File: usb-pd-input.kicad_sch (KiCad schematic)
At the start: 14 parts, among them J1 USB-C, Q1 -30V -4A, U1 STUSB4500QTR

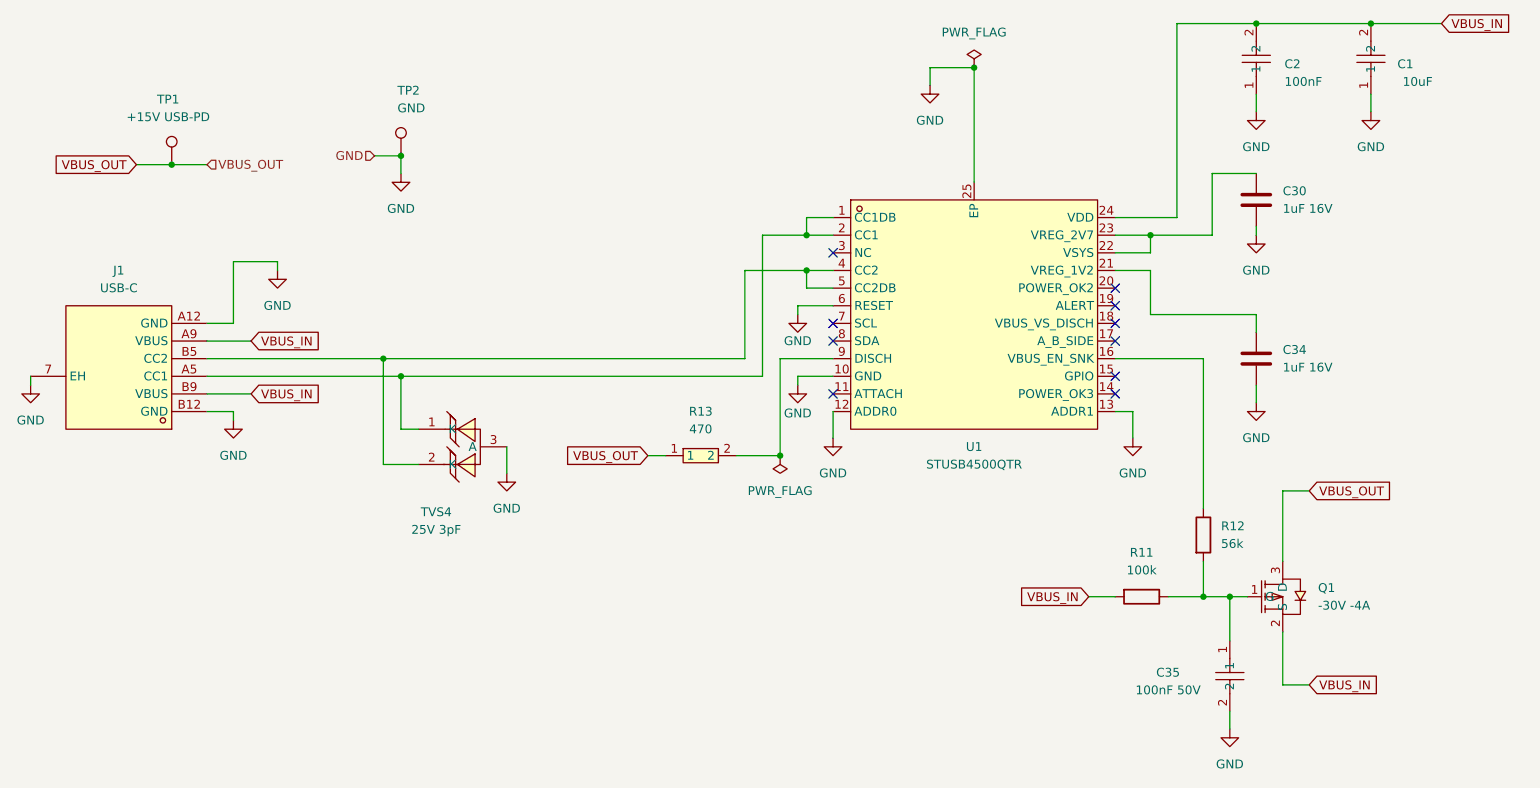
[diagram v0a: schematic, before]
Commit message: fix: Correct project name in hierarchical schematic instances
All sub-sheet instance blocks had inconsistent project names - some used
(project "") while others used (project "zudo-pd"). This caused KiCad to
display "?" for designators when opening sub-sheets.

Changed all instances to use (project "zudo-pd") consistently across:
- usb-pd-input.kicad_sch (16 → 31 fixed)
- dc-dc-conversion.kicad_sch (14 → 49 fixed)
- linear-regulation.kicad_sch (26 → 46 fixed)
- output.kicad_sch (3 → 6 fixed)

Co-Authored-By: Claude <noreply@anthropic.com>
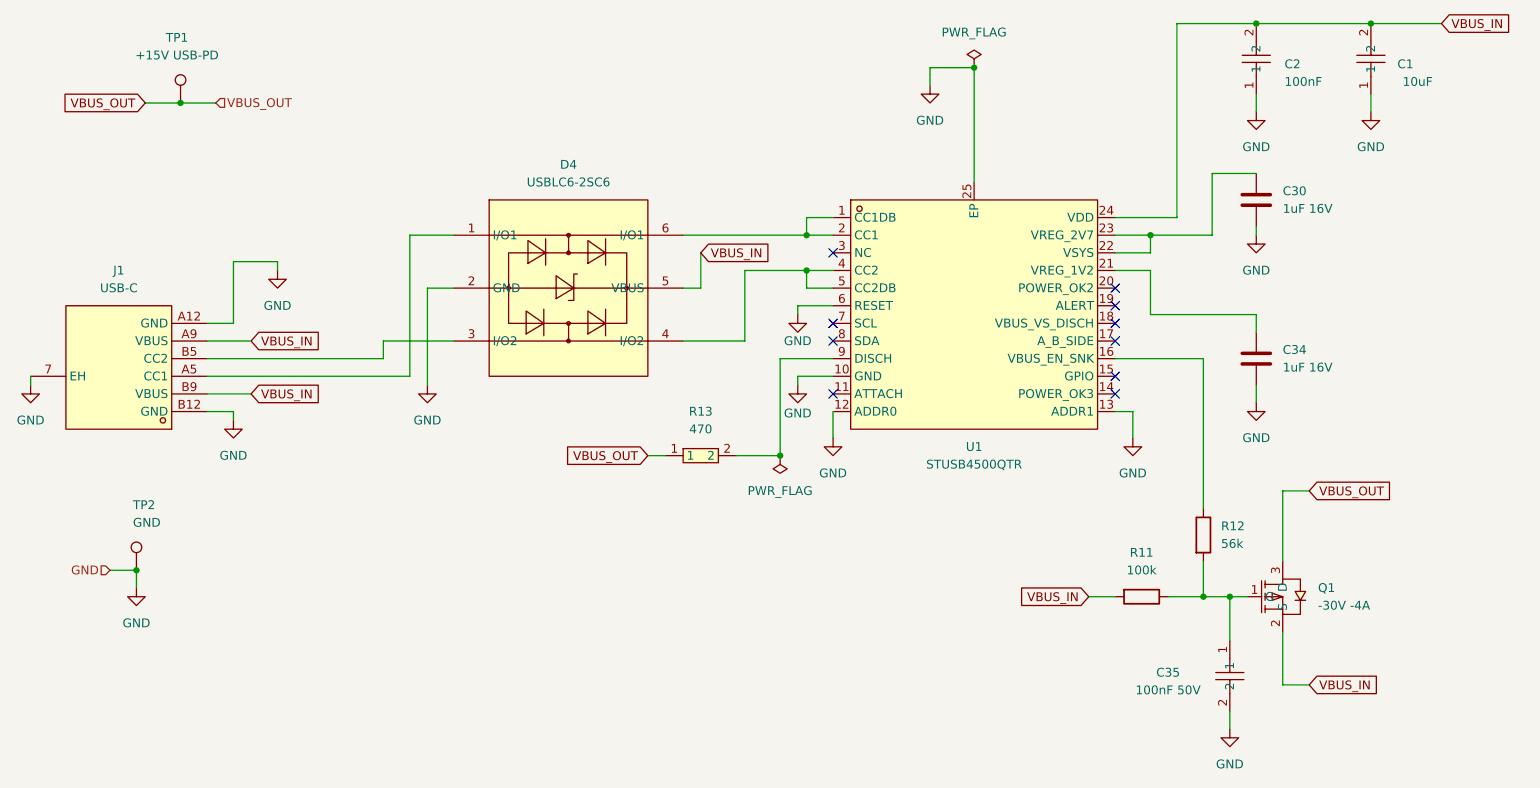
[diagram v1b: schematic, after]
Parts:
- removed TVS4: 25V 3pF, zudo-pd:SOT-23-3_L2.9-W1.6-P1.90-LS2.8-BR, symbol zudo-pd:ESDA25L_C343997
- added D4: USBLC6-2SC6, zudo-pd:SOT-23-6_L2.9-W1.6-P0.95-LS2.8-BL, symbol zudo-pd:USBLC6-2SC6_C7519
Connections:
- net GND: now also D4.2 (GND)
- net VBUS_IN: now also D4.5 (VBUS)
- net at U1.1 (CC1DB), U1.2 (CC1): now also D4.6 (I/O1); no longer J1.A5 (CC1)
- net at U1.4 (CC2), U1.5 (CC2DB): now also D4.4 (I/O2); no longer J1.B5 (CC2)
- new net: D4.1 (I/O1), J1.A5 (CC1)
- new net: D4.3 (I/O2), J1.B5 (CC2)
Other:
- moved on the sheet: TP1, TP2

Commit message: fix: Disconnect VSYS from VREG_2V7 net in KiCad schematic
Remove the incorrect wire connecting VSYS (pin 22) to VREG_2V7 (pin 23)
on the STUSB4500. VSYS is now extended to GND and pin 18 (VBUS_VS_DISCH)
has a no_connect marker added as a placeholder until the series resistor
connection is implemented.

Co-Authored-By: Claude <noreply@anthropic.com>
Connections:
- net at C30.1, U1.23 (VREG_2V7): no longer U1.22 (VSYS)
- no-connect marks 10 -> 11
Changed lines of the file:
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@@
-	)
-	(junction
-		(at 201.93 52.07)
-		(diameter 0)
-		(color 0 0 0 0)
 	)
 	(junction
@@
 	)
 	(no_connect
+		(at 196.85 54.61)
+	)
+	(no_connect
 		(at 196.85 62.23)
 	)
@@
 	(wire
 		(pts
-			(xy 196.85 52.07) (xy 201.93 52.07)
+			(xy 196.85 52.07) (xy 210.82 52.07)
 		)
 		(stroke
@@
 	(wire
 		(pts
-			(xy 201.93 52.07) (xy 201.93 54.61)
-		)
-		(stroke
-			(width 0)
-			(type default)
-		)
-	)
-	(wire
-		(pts
 			(xy 137.16 59.69) (xy 134.62 59.69)
 		)
@@
 	(wire
 		(pts
-			(xy 201.93 52.07) (xy 210.82 52.07)
-		)
-		(stroke
-			(width 0)
-			(type default)
-		)
-	)
-	(wire
-		(pts
 			(xy 196.85 57.15) (xy 201.93 57.15)
 		)
 		(stroke
-			(width 0)
-			(type default)
-		)
-	)
-	(wire
-		(pts
-			(xy 196.85 54.61) (xy 201.93 54.61)
-		)
-		(stroke

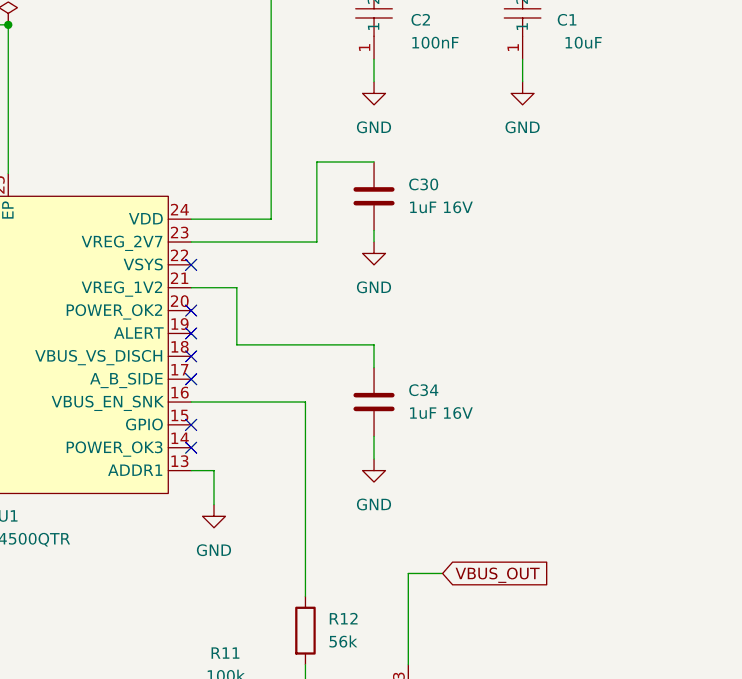
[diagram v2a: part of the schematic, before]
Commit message: docs: Add NVM programming guide and fix LCSC part numbers in schematics
Add comprehensive STUSB4500 NVM programming documentation covering
hardware setup (NUCLEO-F072RB + pogo pin clip), target PDO configuration
(15V/3A), and programming procedure. Fix LCSC part numbers in KiCad
schematics: add missing parts to usb-pd-input components, correct C9
voltage rating from 25V to 50V in dc-dc-conversion.

Co-Authored-By: Claude <noreply@anthropic.com>
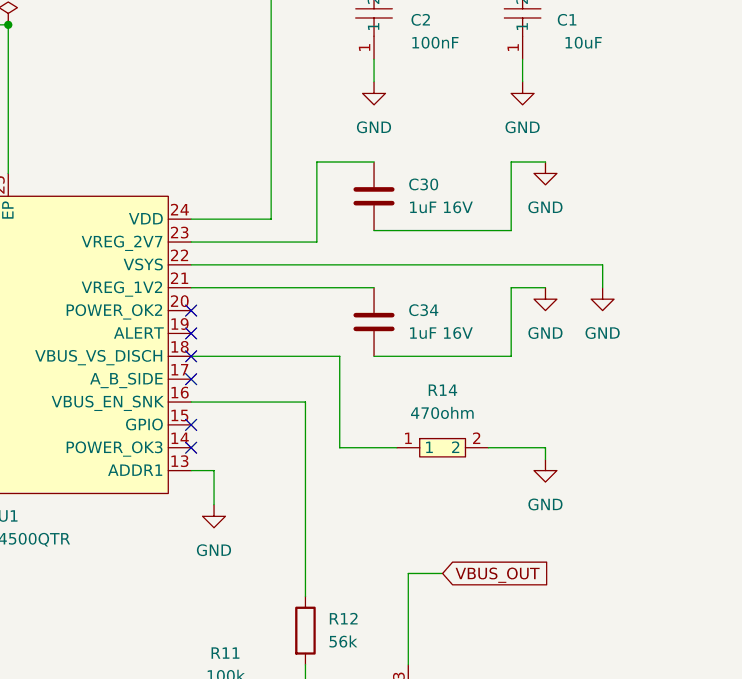
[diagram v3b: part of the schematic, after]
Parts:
- added R14: 470ohm, easyeda2kicad:R0603, symbol zudo-pd:0603WAF4700T5E
- C30, C34: LCSC Part (none) -> C6119849
- R11: LCSC Part (none) -> C14675
- R12: LCSC Part (none) -> C23168
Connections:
- net GND: now also U1.22 (VSYS), R14.2
- net at U1.18 (VBUS_VS_DISCH): now also R14.1
- no-connect marks 11 -> 10
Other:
- moved on the sheet: C34
